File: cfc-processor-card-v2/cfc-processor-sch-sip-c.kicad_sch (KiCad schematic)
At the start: 38 parts, among them J5 DM3BT-DSF-PEJS, U11 TCAN330, U12 SFEM016GB1EA1TO-I-GE-121-STD, U7 OSD3358-1G-ISM

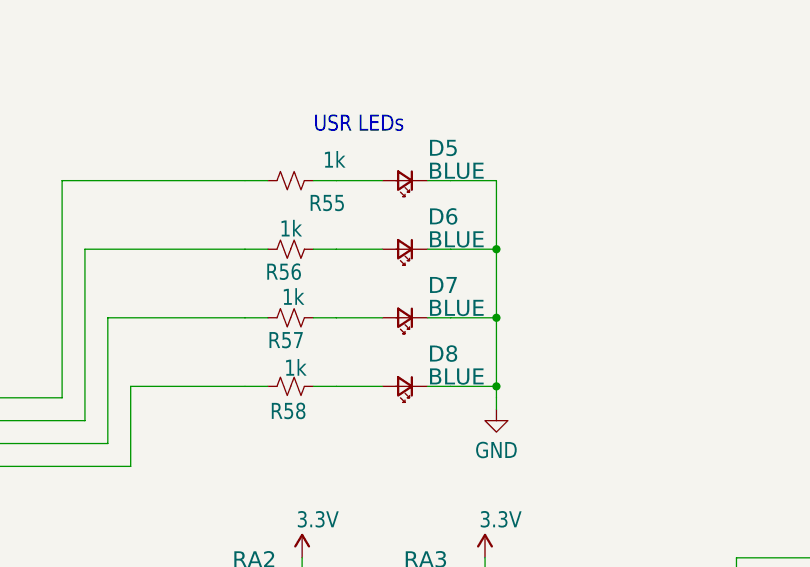
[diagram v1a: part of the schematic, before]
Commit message: Update
Updated BOM, couple of fixes on OPD. Minor routing and layout changes. Removed logic gates from sensor card.
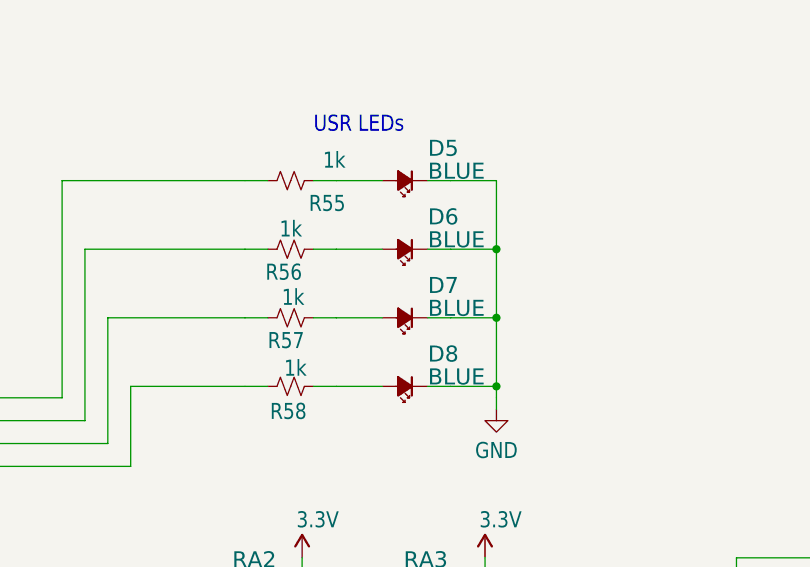
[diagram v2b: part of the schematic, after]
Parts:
- C23, C32: DPN 490-GRT21BC71E106KE13LCT-ND -> 490-GRT21BC71E106KE13KCT-ND; MPN GRT21BC71E106KE13L -> GRT21BC71E106KE13K
- C24, C25: DPN 587-3472-1-ND -> 399-6856-1-ND; MFR Taiyo Yuden -> KEMET; MPN TMK107BJ104KAHT -> C0603C104K5RACAUTO
- C26, C27, C28, C29, C30, C31: DIS DigiKey -> Digikey; DPN 587-3473-1-ND -> 490-10675-2-ND; MFR Taiyo Yuden -> Murata Electronics; MPN TMK107BJ105KAHT -> GCM21BR71H105KA03L
- D5, D6, D7, D8: symbol Device:LED_Small -> Device:LED_Small_Filled
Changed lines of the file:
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@@
 			)
 		)
-		(property "Description" "Unpolarized capacitor, small symbol"
+		(property "Description" "10 µF ±10% 25V Ceramic Capacitor X7S 0805 (2012 Metric)"
 			(at 411.48 130.81 0)
 			(hide yes)
@@
 			)
 		)
-		(property "DPN" "490-GRT21BC71E106KE13LCT-ND"
+		(property "DPN" "490-GRT21BC71E106KE13KCT-ND"
 			(at 411.48 130.81 0)
 			(hide yes)
@@
 			)
 		)
-		(property "MPN" "GRT21BC71E106KE13L"
+		(property "MPN" "GRT21BC71E106KE13K"
 			(at 411.48 130.81 0)
 			(hide yes)
@@
 			)
 		)
-		(property "Description" "Unpolarized capacitor, small symbol"
+		(property "Description" "1 µF ±10% 50V Ceramic Capacitor X7R 0805 (2012 Metric)"
 			(at 388.62 130.81 0)
 			(hide yes)
@@
 			)
 		)
-		(property "DIS" "DigiKey"
+		(property "DIS" "Digikey"
 			(at 388.62 130.81 0)
 			(hide yes)
@@
 			)
 		)
-		(property "DPN" "587-3473-1-ND"
+		(property "DPN" "490-10675-2-ND"
 			(at 388.62 130.81 0)
 			(hide yes)
@@
 			)
 		)
-		(property "MFR" "Taiyo Yuden"
+		(property "MFR" "Murata Electronics"
 			(at 388.62 130.81 0)
 			(hide yes)
@@
 			)
 		)
-		(property "MPN" "TMK107BJ105KAHT"
+		(property "MPN" "GCM21BR71H105KA03L"
 			(at 388.62 130.81 0)
 			(hide yes)
@@
 			)
 		)
-		(property "Description" "Unpolarized capacitor, small symbol"
+		(property "Description" "1 µF ±10% 50V Ceramic Capacitor X7R 0805 (2012 Metric)"
 			(at 381 130.81 0)
 			(hide yes)
@@
 			)
 		)
-		(property "DIS" "DigiKey"
+		(property "DIS" "Digikey"
 			(at 381 130.81 0)
 			(hide yes)
@@
 			)
 		)
-		(property "DPN" "587-3473-1-ND"
+		(property "DPN" "490-10675-2-ND"
 			(at 381 130.81 0)
 			(hide yes)
@@
 			)
 		)
-		(property "MFR" "Taiyo Yuden"
+		(property "MFR" "Murata Electronics"
 			(at 381 130.81 0)
 			(hide yes)
@@
 			)
 		)
-		(property "MPN" "TMK107BJ105KAHT"
+		(property "MPN" "GCM21BR71H105KA03L"
 			(at 381 130.81 0)
 			(hide yes)
@@
 	)
 	(symbol
-		(lib_name "LED_Small_1")
-		(lib_id "Device:LED_Small")
+		(lib_id "Device:LED_Small_Filled")
 		(at 311.15 92.71 180)
 		(unit 1)
@@
 			)
 		)
-		(property "Description" "Light emitting diode, small symbol"
+		(property "Description" "Light emitting diode, small symbol, filled shape"
 			(at 311.15 92.71 0)
 			(hide yes)
@@
 			)
 		)
-		(property "Description" "Unpolarized capacitor, small symbol"
+		(property "Description" "0.1 µF ±10% 50V Ceramic Capacitor X7R 0603 (1608 Metric)"
 			(at 29.21 147.32 0)
 			(hide yes)
@@
 			)
 		)
-		(property "DPN" "587-3472-1-ND"
+		(property "DPN" "399-6856-1-ND"
 			(at 29.21 147.32 0)
 			(hide yes)
@@
 			)
 		)
-		(property "MFR" "Taiyo Yuden"
+		(property "MFR" "KEMET"
 			(at 29.21 147.32 0)
 			(hide yes)
@@
 			)
 		)
-		(property "MPN" "TMK107BJ104KAHT"
+		(property "MPN" "C0603C104K5RACAUTO"
 			(at 29.21 147.32 0)
 			(hide yes)
@@
 			)
 		)
-		(property "Description" "Unpolarized capacitor, small symbol"
+		(property "Description" "1 µF ±10% 50V Ceramic Capacitor X7R 0805 (2012 Metric)"
 			(at 396.24 130.81 0)
 			(hide yes)
@@
 			)
 		)
-		(property "DIS" "DigiKey"
+		(property "DIS" "Digikey"
 			(at 396.24 130.81 0)
 			(hide yes)
@@
 			)
 		)
-		(property "DPN" "587-3473-1-ND"
+		(property "DPN" "490-10675-2-ND"
 			(at 396.24 130.81 0)
 			(hide yes)
@@
 			)
 		)
-		(property "MFR" "Taiyo Yuden"
+		(property "MFR" "Murata Electronics"
 			(at 396.24 130.81 0)
 			(hide yes)
@@
 			)
 		)
-		(property "MPN" "TMK107BJ105KAHT"
+		(property "MPN" "GCM21BR71H105KA03L"
 			(at 396.24 130.81 0)
 			(hide yes)
@@
 			)
 		)
-		(property "Description" "Unpolarized capacitor, small symbol"
+		(property "Description" "0.1 µF ±10% 50V Ceramic Capacitor X7R 0603 (1608 Metric)"
 			(at 234.95 33.02 0)
 			(hide yes)
@@
 			)
 		)
-		(property "DPN" "587-3472-1-ND"
+		(property "DPN" "399-6856-1-ND"
 			(at 234.95 33.02 0)
 			(hide yes)
@@
 			)
 		)
-		(property "MFR" "Taiyo Yuden"
+		(property "MFR" "KEMET"
 			(at 234.95 33.02 0)
 			(hide yes)
@@
 			)
 		)
-		(property "MPN" "TMK107BJ104KAHT"
+		(property "MPN" "C0603C104K5RACAUTO"
 			(at 234.95 33.02 0)
 			(hide yes)
@@
 			)
 		)
-		(property "Description" "Unpolarized capacitor, small symbol"
+		(property "Description" "10 µF ±10% 25V Ceramic Capacitor X7S 0805 (2012 Metric)"
 			(at 19.05 147.32 0)
 			(hide yes)
@@
 			)
 		)
-		(property "DPN" "490-GRT21BC71E106KE13LCT-ND"
+		(property "DPN" "490-GRT21BC71E106KE13KCT-ND"
 			(at 19.05 147.32 0)
 			(hide yes)
@@
 			)
 		)
-		(property "MPN" "GRT21BC71E106KE13L"
+		(property "MPN" "GRT21BC71E106KE13K"
 			(at 19.05 147.32 0)
 			(hide yes)
@@
 	)
 	(symbol
-		(lib_id "Device:LED_Small")
+		(lib_id "Device:LED_Small_Filled")
 		(at 311.15 85.09 180)
 		(unit 1)
@@
 			)
 		)
-		(property "Description" "Light emitting diode, small symbol"
+		(property "Description" "Light emitting diode, small symbol, filled shape"
 			(at 311.15 85.09 0)
 			(hide yes)
@@
 	)
 	(symbol
-		(lib_name "LED_Small_1")
-		(lib_id "Device:LED_Small")
+		(lib_id "Device:LED_Small_Filled")
 		(at 311.15 107.95 180)
 		(unit 1)
@@
 			)
 		)
-		(property "Description" "Light emitting diode, small symbol"
+		(property "Description" "Light emitting diode, small symbol, filled shape"
 			(at 311.15 107.95 0)
 			(hide yes)
@@
 			)
 		)
-		(property "Description" "Unpolarized capacitor, small symbol"
+		(property "Description" "1 µF ±10% 50V Ceramic Capacitor X7R 0805 (2012 Metric)"
 			(at 367.03 133.35 0)
 			(hide yes)
@@
 			)
 		)
-		(property "DIS" "DigiKey"
+		(property "DIS" "Digikey"
 			(at 367.03 133.35 0)
 			(hide yes)
@@
 			)
 		)
-		(property "DPN" "587-3473-1-ND"
+		(property "DPN" "490-10675-2-ND"
 			(at 367.03 133.35 0)
 			(hide yes)
@@
 			)
 		)
-		(property "MFR" "Taiyo Yuden"
+		(property "MFR" "Murata Electronics"
 			(at 367.03 133.35 0)
 			(hide yes)
@@
 			)
 		)
-		(property "MPN" "TMK107BJ105KAHT"
+		(property "MPN" "GCM21BR71H105KA03L"
 			(at 367.03 133.35 0)
 			(hide yes)
@@
 			)
 		)
-		(property "Description" "Unpolarized capacitor, small symbol"
+		(property "Description" "1 µF ±10% 50V Ceramic Capacitor X7R 0805 (2012 Metric)"
 			(at 403.86 130.81 0)
 			(hide yes)
@@
 			)
 		)
-		(property "DIS" "DigiKey"
+		(property "DIS" "Digikey"
 			(at 403.86 130.81 0)
 			(hide yes)
@@
 			)
 		)
-		(property "DPN" "587-3473-1-ND"
+		(property "DPN" "490-10675-2-ND"
 			(at 403.86 130.81 0)
 			(hide yes)
@@
 			)
 		)
-		(property "MFR" "Taiyo Yuden"
+		(property "MFR" "Murata Electronics"
 			(at 403.86 130.81 0)
 			(hide yes)
@@
 			)
 		)
-		(property "MPN" "TMK107BJ105KAHT"
+		(property "MPN" "GCM21BR71H105KA03L"
 			(at 403.86 130.81 0)
 			(hide yes)
@@
 	)
 	(symbol
-		(lib_name "LED_Small_2")
-		(lib_id "Device:LED_Small")
+		(lib_id "Device:LED_Small_Filled")
 		(at 311.15 100.33 180)
 		(unit 1)
@@
 			)
 		)
-		(property "Description" "Light emitting diode, small symbol"
+		(property "Description" "Light emitting diode, small symbol, filled shape"
 			(at 311.15 100.33 0)
 			(hide yes)
@@
 			)
 		)
-		(property "Description" "Unpolarized capacitor, small symbol"
+		(property "Description" "1 µF ±10% 50V Ceramic Capacitor X7R 0805 (2012 Metric)"
 			(at 359.41 133.35 0)
 			(hide yes)
@@
 			)
 		)
-		(property "DIS" "DigiKey"
+		(property "DIS" "Digikey"
 			(at 359.41 133.35 0)
 			(hide yes)
@@
 			)
 		)
-		(property "DPN" "587-3473-1-ND"
+		(property "DPN" "490-10675-2-ND"
 			(at 359.41 133.35 0)
 			(hide yes)
@@
 			)
 		)
-		(property "MFR" "Taiyo Yuden"
+		(property "MFR" "Murata Electronics"
 			(at 359.41 133.35 0)
 			(hide yes)
@@
 			)
 		)
-		(property "MPN" "TMK107BJ105KAHT"
+		(property "MPN" "GCM21BR71H105KA03L"
 			(at 359.41 133.35 0)
 			(hide yes)
